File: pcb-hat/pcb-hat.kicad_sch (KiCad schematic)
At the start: 65 parts, among them Q1 NTMFS5C468NLT1G, Q2 Q_NPN, Q3 Q_PMOS_GSD, U1 AOZ6605PI-1, U2 INA219AxD, U3 INA219AxD, U4 HTD Servo, U5 Vertical_Pi_Breakout, U6 Power_Connector, U7 AOZ6605PI-1, U8 Horizontal_Pi_Breakout, U9 Raspberry_Pi_Generic

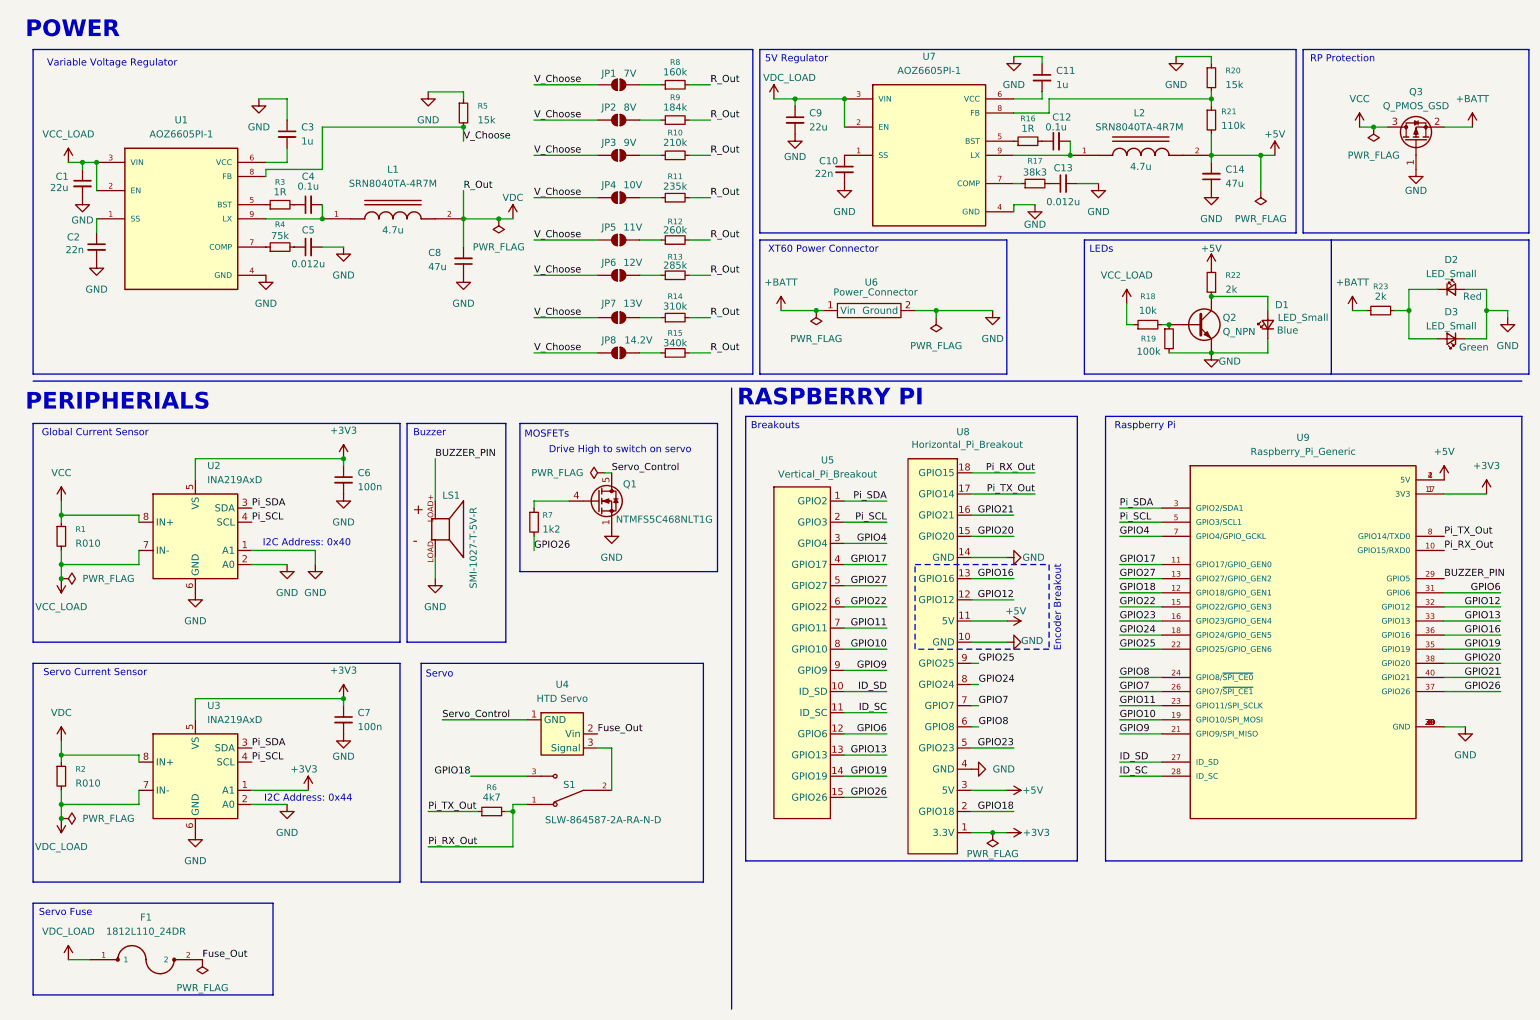
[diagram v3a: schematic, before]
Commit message: WIP: Fix footprints, add new jumper pad, 3d models. Begin routing
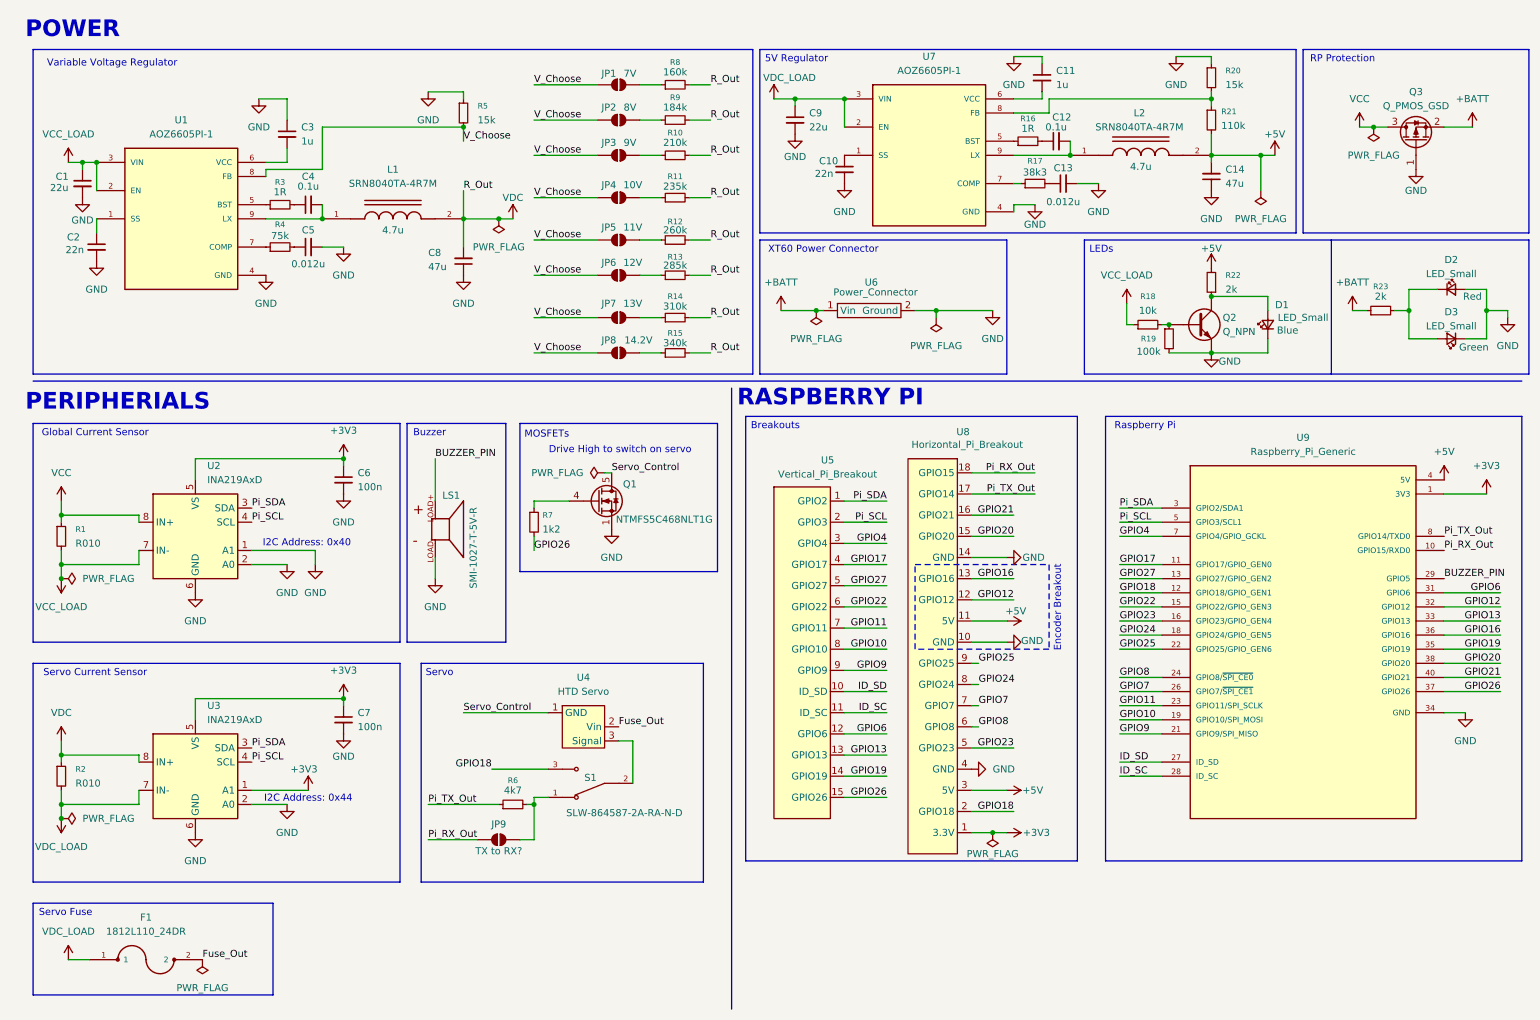
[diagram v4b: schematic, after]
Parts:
- added JP9: TX to RX?, Jumper:SolderJumper-2_P1.3mm_Open_RoundedPad1.0x1.5mm, symbol Jumper:SolderJumper_2_Open
- U5: footprint Connector_PinHeader_2.54mm:PinHeader_1x15_P2.54mm_Vertical -> pcb_hat:vertical_pi_breakout
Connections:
- net GND: now also Q2.2 (E), U9.14 (GND); no longer Q2.E
- net Pi_RX_Out: now also JP9.1 (A); no longer R6.2, S1.1
- net at D1.2 (A), R22.1: now also Q2.3 (C); no longer Q2.C
- net at R18.2, R19.1: now also Q2.1 (B); no longer Q2.B
- new net: JP9.2 (B), R6.2, S1.1
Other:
- moved on the sheet: R6, S1, U4

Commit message: Finish PCB design v0.1
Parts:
- removed S1: SLW-864587-2A-RA-N-D, pcb_hat:SW_SLW-864587-2A-RA-N-D, symbol PiHatComponents:SLW-864587-2A-RA-N-D
- removed U5: Vertical_Pi_Breakout, pcb_hat:vertical_pi_breakout, symbol PiHatComponents:vertical_pi_breakout
- removed U8: Horizontal_Pi_Breakout, pcb_hat:horizontal_breakout_footprint, symbol PiHatComponents:horizontal_pi_breakout
- added JP2: Servo Selector, Jumper:SolderJumper-3_P1.3mm_Open_RoundedPad1.0x1.5mm, symbol Jumper:SolderJumper_3_Open
- C1, C12, C4, C9: footprint Capacitor_SMD:C_0603_1608Metric -> Capacitor_SMD:C_0603_1608Metric_Pad1.08x0.95mm_HandSolder
- JP1: renamed from JP9; Function (none) -> TX-RX
- R1, R16, R17, R2, R3, R4: footprint Resistor_SMD:R_0603_1608Metric -> Resistor_SMD:R_0603_1608Metric_Pad0.98x0.95mm_HandSolder
- renumbered JP8 to JP10, JP1 to JP3, JP2 to JP4, JP3 to JP5, JP4 to JP6, JP5 to JP7, JP6 to JP8, JP7 to JP9, R7 to R6, R6 to R7, U6 to U5, U7 to U6, U9 to U7
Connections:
- net GPIO18: now also JP2.3 (B)
- net at JP1.2 (B), R7.2: now also JP2.1 (A)
- net at U4.3 (Signal): now also JP2.2 (C)
- net GPIO10: no longer names the net of U7.19 (GPIO10/SPI_MOSI)
- net GPIO11: no longer names the net of U7.23 (GPIO11/SPI_SCLK)
- net GPIO12: no longer names the net of U7.32 (GPIO12)
- net GPIO13: no longer names the net of U7.33 (GPIO13)
- net GPIO16: no longer names the net of U7.36 (GPIO16)
- net GPIO17: no longer names the net of U7.11 (GPIO17/GPIO_GEN0)
- net GPIO19: no longer names the net of U7.35 (GPIO19)
- net GPIO20: no longer names the net of U7.38 (GPIO20)
- net GPIO21: no longer names the net of U7.40 (GPIO21)
- net GPIO22: no longer names the net of U7.15 (GPIO22/GPIO_GEN3)
- net GPIO23: no longer names the net of U7.16 (GPIO23/GPIO_GEN4)
- net GPIO24: no longer names the net of U7.18 (GPIO24/GPIO_GEN5)
- net GPIO25: no longer names the net of U7.22 (GPIO25/GPIO_GEN6)
- net GPIO27: no longer names the net of U7.13 (GPIO27/GPIO_GEN2)
- net GPIO4: no longer names the net of U7.7 (GPIO4/GPIO_GCKL)
- net GPIO6: no longer names the net of U7.31 (GPIO6)
- net GPIO7: no longer names the net of U7.26 (GPIO7/~{SPI_CE1})
- net GPIO8: no longer names the net of U7.24 (GPIO8/~{SPI_CE0})
- net GPIO9: no longer names the net of U7.21 (GPIO9/SPI_MISO)
- net ID_SC: no longer names the net of U7.28 (ID_SC)
- net ID_SD: no longer names the net of U7.27 (ID_SD)
- no-connect marks 0 -> 21
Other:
- note removed: "Breakouts"
- note removed: "Encoder Breakout"
- title: AirHat -> Airbender
- moved on the sheet: JP1, LS1, Q1, R6, R7, U4

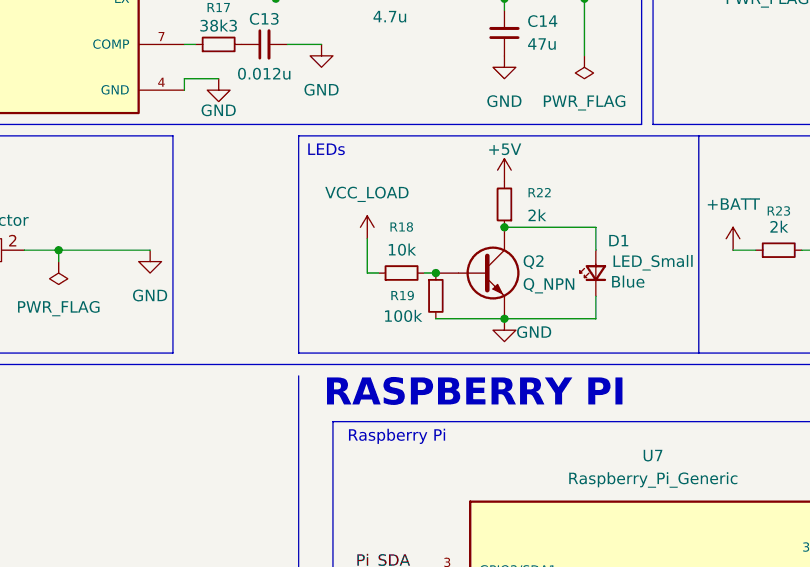
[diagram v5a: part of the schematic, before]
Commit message: Fix blue LED not turning on
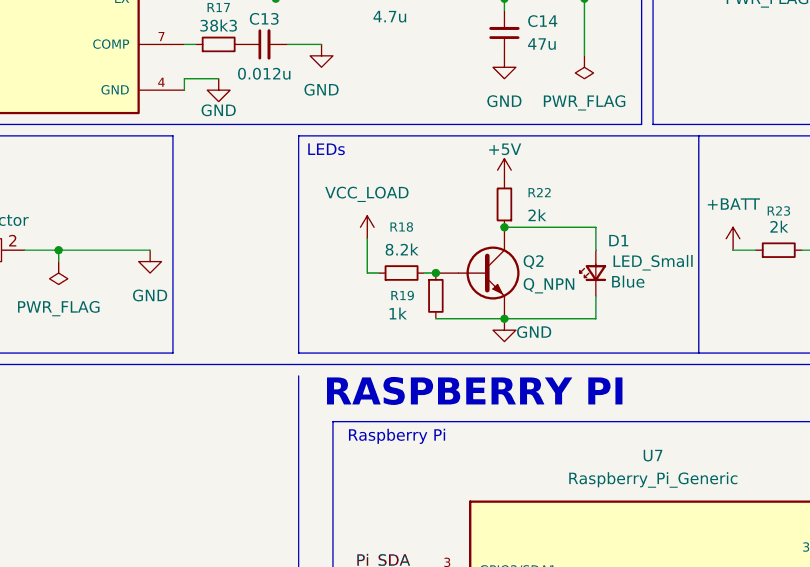
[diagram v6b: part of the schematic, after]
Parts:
- R18: value 10k -> 8.2k
- R19: value 100k -> 1k
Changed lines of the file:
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@@
 			)
 		)
-		(property "Value" "10k"
+		(property "Value" "8.2k"
 			(at 214.63 66.04 90)
 			(effects
@@
 			)
 		)
-		(property "Value" "100k"
-			(at 212.598 73.406 0)
+		(property "Value" "1k"
+			(at 213.106 73.152 0)
 			(effects
 				(font

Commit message: Change digikey PN for resistors
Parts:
- R18: Digikey PN RC0603FR-0710KL -> 311-8.2KGRCT-ND
- R19: Digikey PN RC0603FR-07100KL -> RMCF0603FT1K00CT-ND
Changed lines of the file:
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@@
 	(title_block
 		(title "Airbender")
-		(date "2025-12-24")
-		(rev "0.1.0")
+		(date "2026-01-11")
+		(rev "0.1.1")
 		(comment 1 "Made by Harshil M, Seth O")
 	)
@@
 			)
 		)
-		(property "Digikey PN" "RC0603FR-0710KL"
+		(property "Digikey PN" "311-8.2KGRCT-ND"
 			(at 214.63 68.58 90)
 			(effects
@@
 			)
 		)
-		(property "Digikey PN" "RC0603FR-07100KL"
+		(property "Digikey PN" "RMCF0603FT1K00CT-ND"
 			(at 218.44 71.12 0)
 			(effects
